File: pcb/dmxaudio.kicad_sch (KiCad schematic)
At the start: 11 parts, among them J1 USB_A, J2 RJ45_Bel_SI-60062-F, J3 RJ45, SW1 SW_DIP_x09, SW2 SW_DPDT_x2, U1 Teensy4.1, U2 SN65HVD11HD

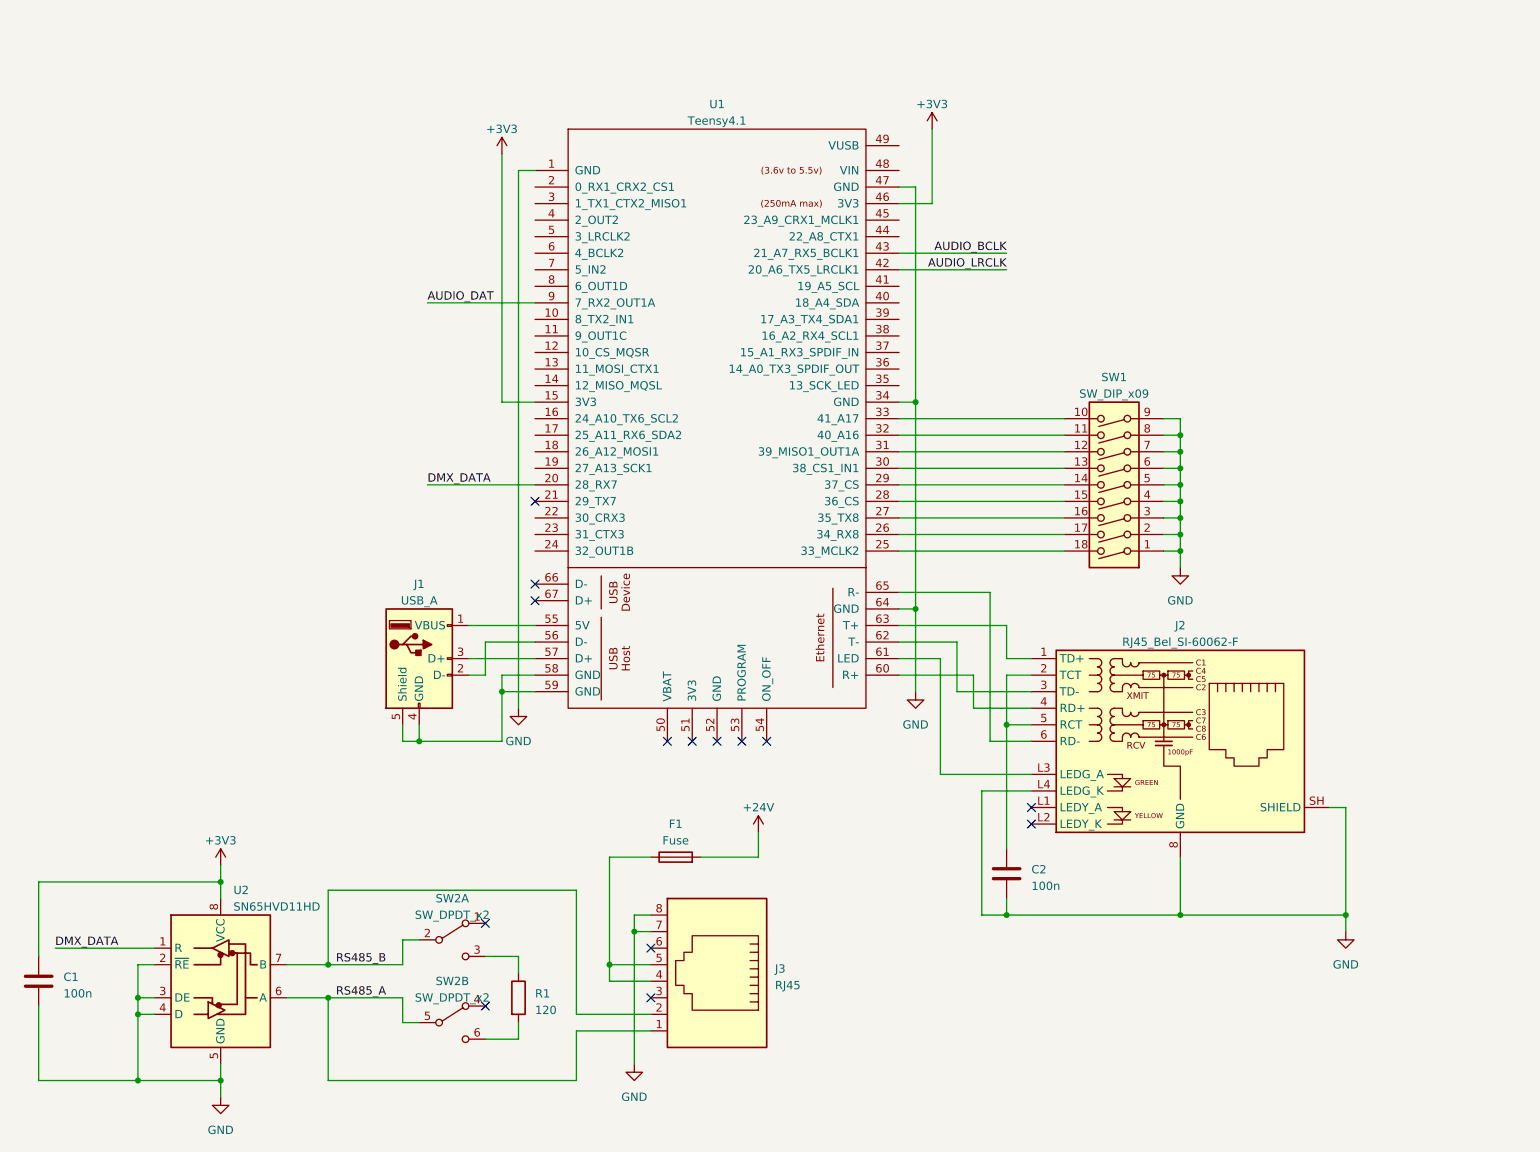
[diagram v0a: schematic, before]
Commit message: Starting to clean up schematic and split into multiple sheets
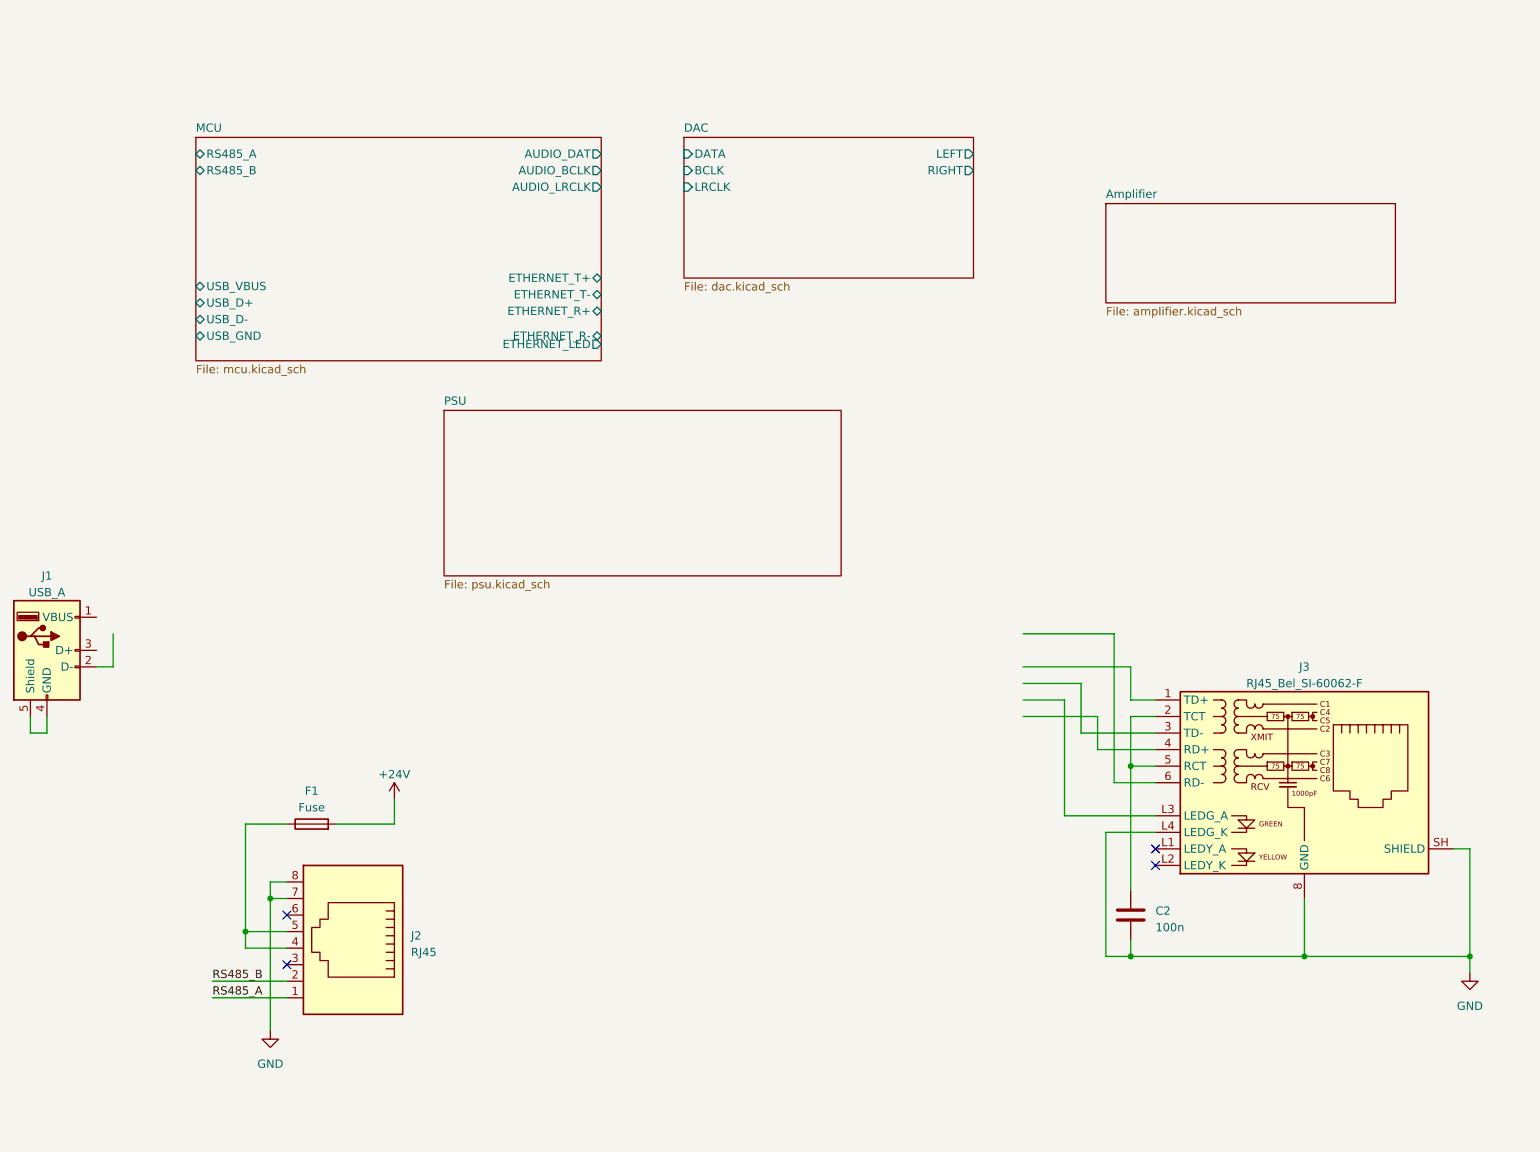
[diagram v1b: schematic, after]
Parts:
- removed C1: 100n, Capacitor_SMD:C_0603_1608Metric_Pad1.08x0.95mm_HandSolder, symbol Device:C
- removed J2: RJ45_Bel_SI-60062-F, Connector_RJ:RJ45_Bel_SI-60062-F, symbol Connector:RJ45_Bel_SI-60062-F
- removed J3: RJ45, Connector_RJ:RJ45_Amphenol_54602-x08_Horizontal, symbol Connector:RJ45
- removed R1: 120, Resistor_SMD:R_0603_1608Metric_Pad0.98x0.95mm_HandSolder, symbol Device:R
- removed SW1: SW_DIP_x09, Button_Switch_THT:SW_DIP_SPSTx09_Slide_9.78x25.04mm_W7.62mm_P2.54mm, symbol Switch:SW_DIP_x09
- removed SW2: SW_DPDT_x2, Button_Switch_THT:SW_CuK_JS202011CQN_DPDT_Straight, symbol Switch:SW_DPDT_x2
- removed U1: Teensy4.1, teensy:Teensy41, symbol teensy:Teensy4.1
- removed U2: SN65HVD11HD, Package_SO:SOIC-8_3.9x4.9mm_P1.27mm, symbol Interface_UART:SN65HVD11HD
- added J2: RJ45, Connector_RJ:RJ45_Amphenol_54602-x08_Horizontal, symbol Connector:RJ45
- added J3: RJ45_Bel_SI-60062-F, Connector_RJ:RJ45_Bel_SI-60062-F, symbol Connector:RJ45_Bel_SI-60062-F
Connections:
- net GND: now also J2.7, J2.8, J3.8 (GND), J3.L4 (LEDG_K), J3.SH (SHIELD)
- net RS485_A: now also J2.1
- net RS485_B: now also J2.2
- net at F1.1: now also J2.4, J2.5
- net at C2.1: now also J3.2 (TCT), J3.5 (RCT)
- no-connect marks 14 -> 4
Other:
- added sheet Amplifier (amplifier.kicad_sch)
- added sheet DAC (dac.kicad_sch)
- added sheet MCU (mcu.kicad_sch)
- added sheet PSU (psu.kicad_sch)

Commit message: Updating schematic based on review from Mike
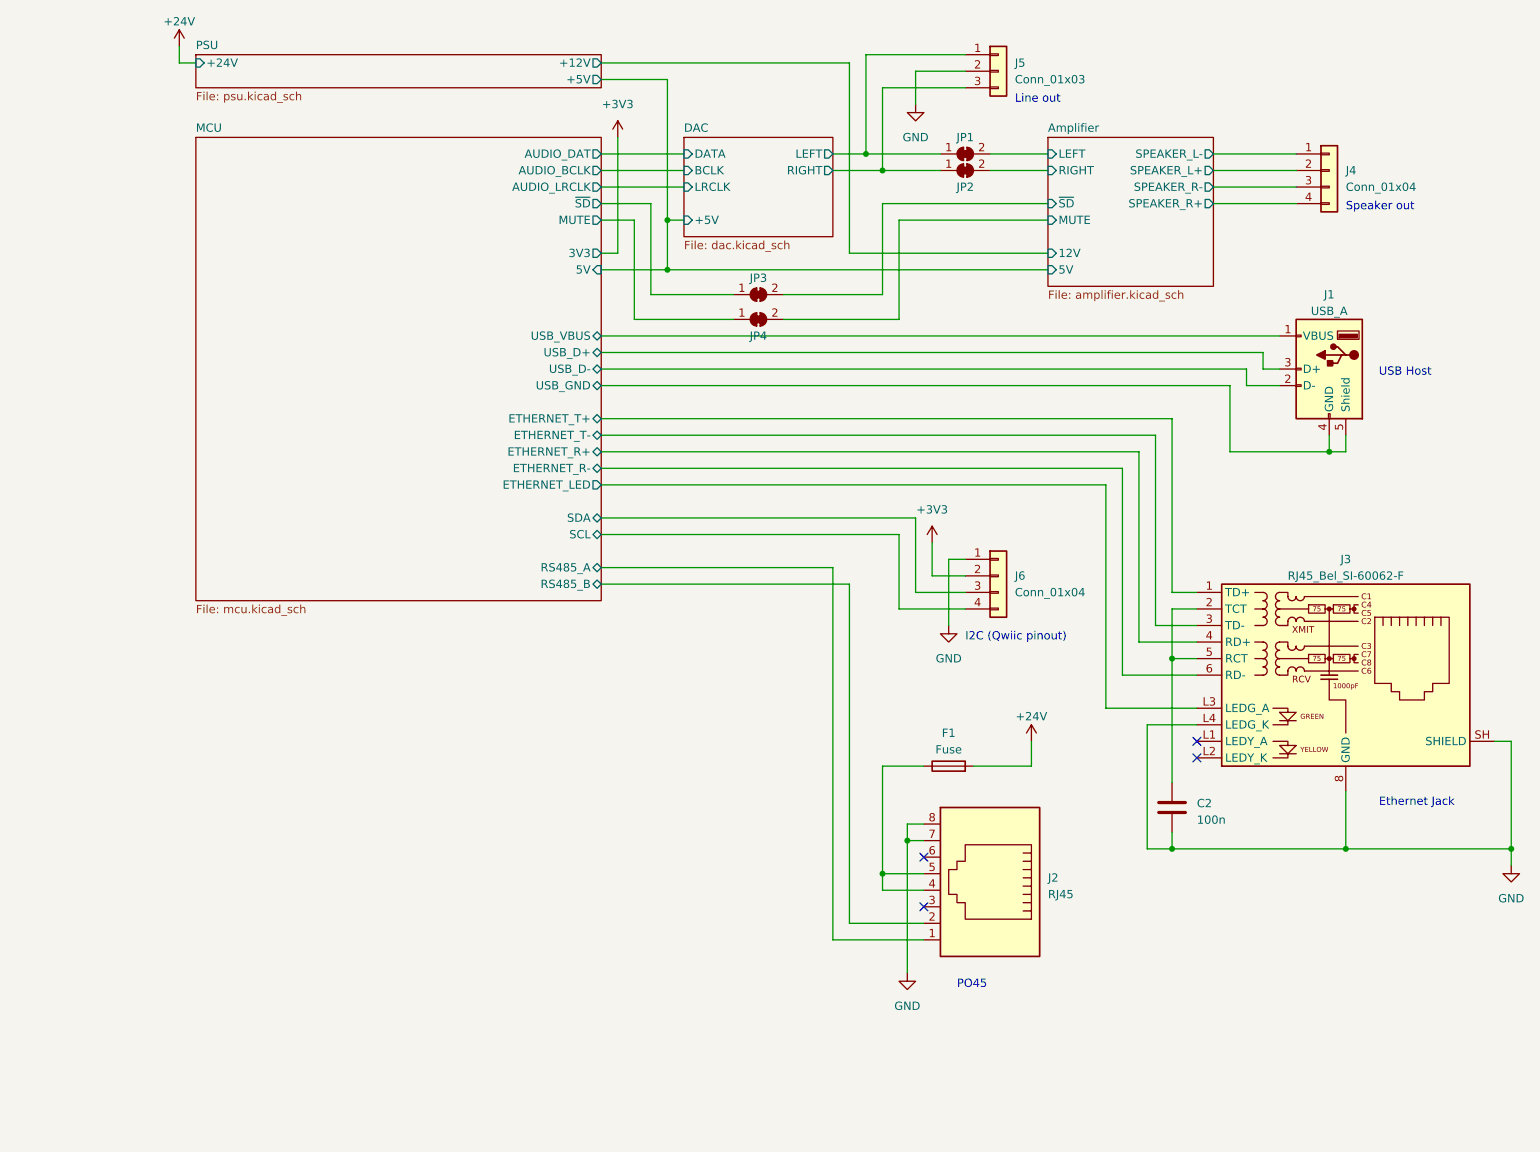
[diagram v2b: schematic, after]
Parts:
- added J4, J6: Conn_01x04, Connector_Molex:Molex_KK-254_AE-6410-04A_1x04_P2.54mm_Vertical, symbol Connector_Generic:Conn_01x04
- added J5: Conn_01x03, Connector_Molex:Molex_KK-254_AE-6410-03A_1x03_P2.54mm_Vertical, symbol Connector_Generic:Conn_01x03
- added JP1, JP2, JP3, JP4: SolderJumper_2_Bridged, Jumper:SolderJumper-2_P1.3mm_Bridged_RoundedPad1.0x1.5mm, symbol Jumper:SolderJumper_2_Bridged
- F1: footprint (none) -> Fuse:Fuseholder_Clip-5x20mm_Keystone_3517_Inline_P23.11x6.76mm_D1.70mm_Horizontal
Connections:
- net RS485_A is gone; now on net MCU/RS485_A: J2.1
- net RS485_B is gone; now on net MCU/RS485_B: J2.2
- net DAC/LEFT: now also J5.1 (Pin_1), JP1.1 (A)
- net DAC/RIGHT: now also J5.3 (Pin_3), JP2.1 (A)
- net GND: now also J5.2 (Pin_2), J6.1 (Pin_1)
- net MCU/ETHERNET_LED: now also J3.L3 (LEDG_A)
- net MCU/ETHERNET_R+: now also J3.4 (RD+)
- net MCU/ETHERNET_R-: now also J3.6 (RD-)
- net MCU/ETHERNET_T+: now also J3.1 (TD+)
- net MCU/ETHERNET_T-: now also J3.3 (TD-)
- net MCU/USB_D+: now also J1.3 (D+)
- net MCU/USB_D-: now also J1.2 (D-)
- net MCU/USB_GND: now also J1.4 (GND), J1.5 (Shield)
- net MCU/USB_VBUS: now also J1.1 (VBUS)
- new net +3V3: J6.2 (Pin_2)
- new net Amplifier/LEFT: JP1.2 (B)
- new net Amplifier/MUTE: JP4.2 (B)
- new net Amplifier/RIGHT: JP2.2 (B)
- new net Amplifier/SPEAKER_L+: J4.2 (Pin_2)
- new net Amplifier/SPEAKER_L-: J4.1 (Pin_1)
- new net Amplifier/SPEAKER_R+: J4.4 (Pin_4)
- new net Amplifier/SPEAKER_R-: J4.3 (Pin_3)
- new net Amplifier/~{SD}: JP3.2 (B)
- new net MCU/MUTE: JP4.1 (A)
- new net MCU/SCL: J6.4 (Pin_4)
- new net MCU/SDA: J6.3 (Pin_3)
- new net MCU/~{SD}: JP3.1 (A)
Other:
- sheet Amplifier ports: added 12V, 5V, LEFT, MUTE, RIGHT, SPEAKER_L+, SPEAKER_L-, SPEAKER_R+, SPEAKER_R-, ~{SD}; removed none
- sheet DAC ports: added +5V; removed none
- sheet MCU ports: added 3V3, 5V, MUTE, SCL, SDA, ~{SD}; removed none
- sheet PSU ports: added +12V, +24V, +5V; removed none
- note added: "Ethernet Jack"
- note added: "I2C (Qwiic pinout)"
- note added: "Line out"
- note added: "PO45"
- note added: "Speaker out"
- note added: "USB Host"
- moved on the sheet: C2, F1, J1, J2, J3
